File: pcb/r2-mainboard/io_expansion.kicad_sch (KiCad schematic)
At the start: 16 parts, among them J22 HC-FPC-05-09-6RLTAG, J23 HC-FPC-05-09-6RLTAG, J28 USB-C 16P, U54 TPS22914BYFPR, U55 TPS22914BYFPR, U56 TPS2553DBVR, U57 USBLC6-2SC6

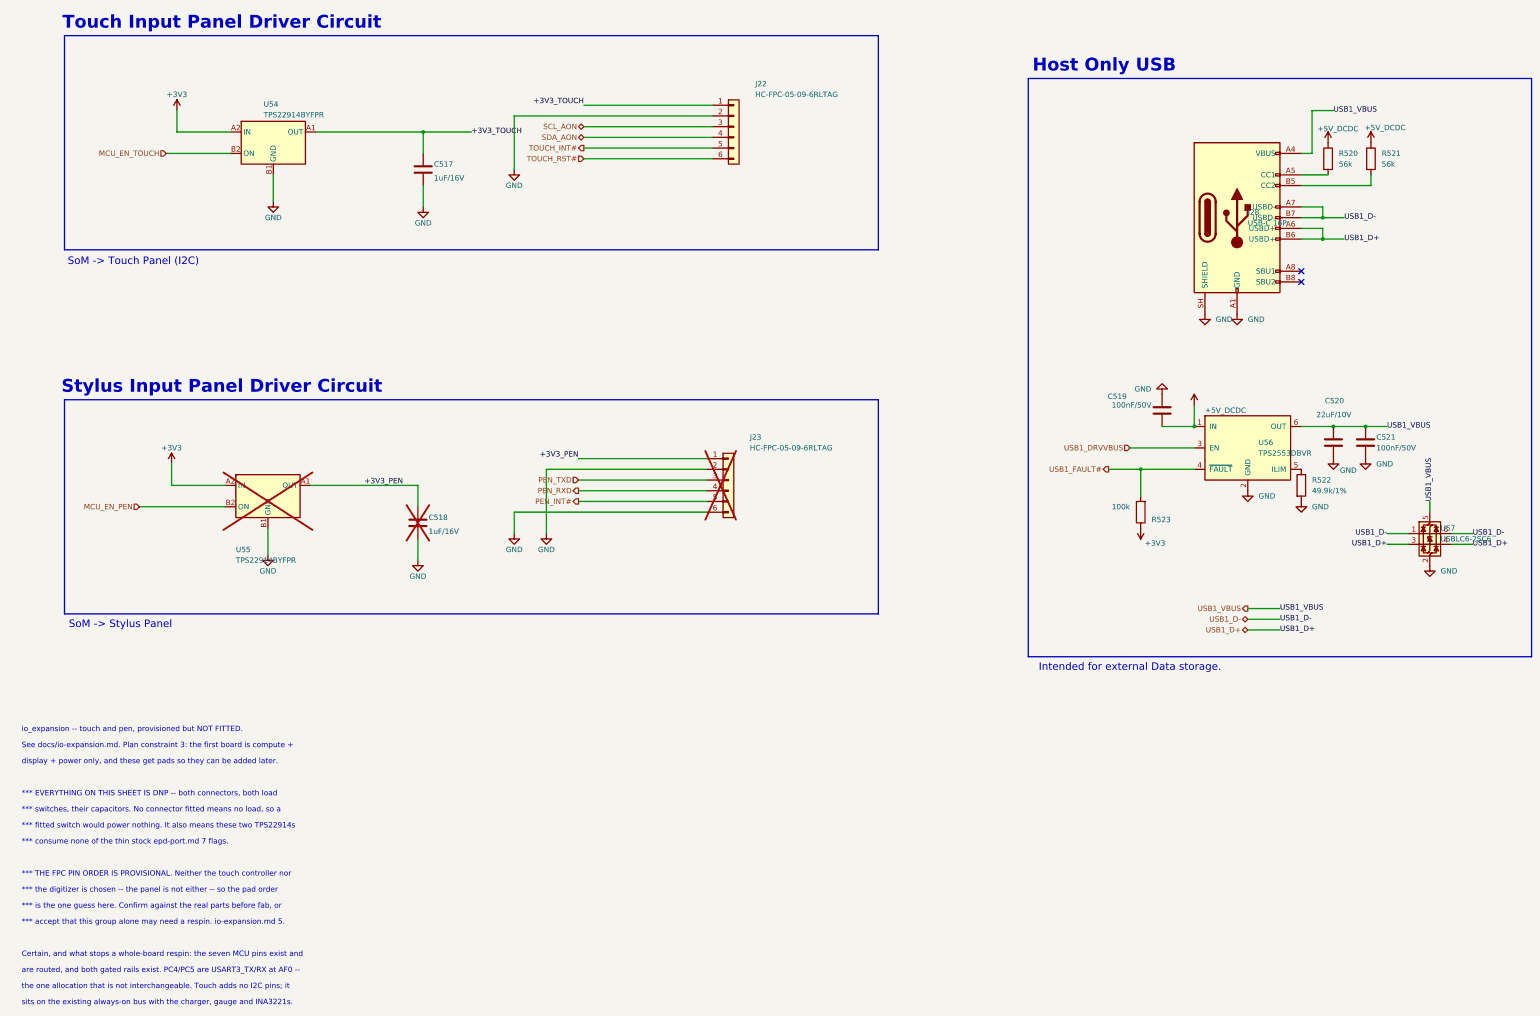
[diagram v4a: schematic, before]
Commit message: Renumber io_expansion to the page-14 scheme
The owner's designator scheme is classifier + sheet page number + a
two-digit part number, counted from 00 -- battery (page 2) is U200/J201,
power (page 3) is U300-U304, fpga_config (page 9) is U902. Pages 10-14
therefore need four digits, which the owner confirmed.

io_expansion is page 14:

  U54  -> U1400   touch load switch      J22  -> J1400   touch FPC
  U55  -> U1401   pen load switch        J23  -> J1401   pen FPC
  U56  -> U1402   TPS2553 USB switch     J28  -> J1402   USB-C host
  U57  -> U1403   USBLC6 ESD
  R520 -> R1400   CC1 pull-up            C517 -> C1400   touch rail
  R521 -> R1401   CC2 pull-up            C518 -> C1401   pen rail
  R522 -> R1402   ILIM                   C519 -> C1402   TPS2553 IN
  R523 -> R1403   FAULT pull-up          C520 -> C1403   VBUS bulk
                                         C521 -> C1404   VBUS bypass

Applied to io_expansion.kicad_sch and r2.kicad_pcb by quoted-string
match, and to the docs and tools/ by word boundary so R52 could never
eat R520. All sixteen target designators were checked free first.

Verified: 519 nets before and after, and *no* net membership changed --
the only differences are the five auto-generated names that embed a
designator (Net-(J28-CC1) -> Net-(J1402-CC1) and friends). ERC unchanged
at 14 errors / 20 warnings. Schematic and board designators agree in
both directions.

The scheme is now recorded in CLAUDE.md, including the warning that
check_pcb.py and check_ucf.py still assert on legacy names.

Co-Authored-By: Claude Opus 5 <noreply@anthropic.com>
Claude-Session: https://claude.ai/code/session_01MHTAe6ZnhogTEgtyPcLhwG
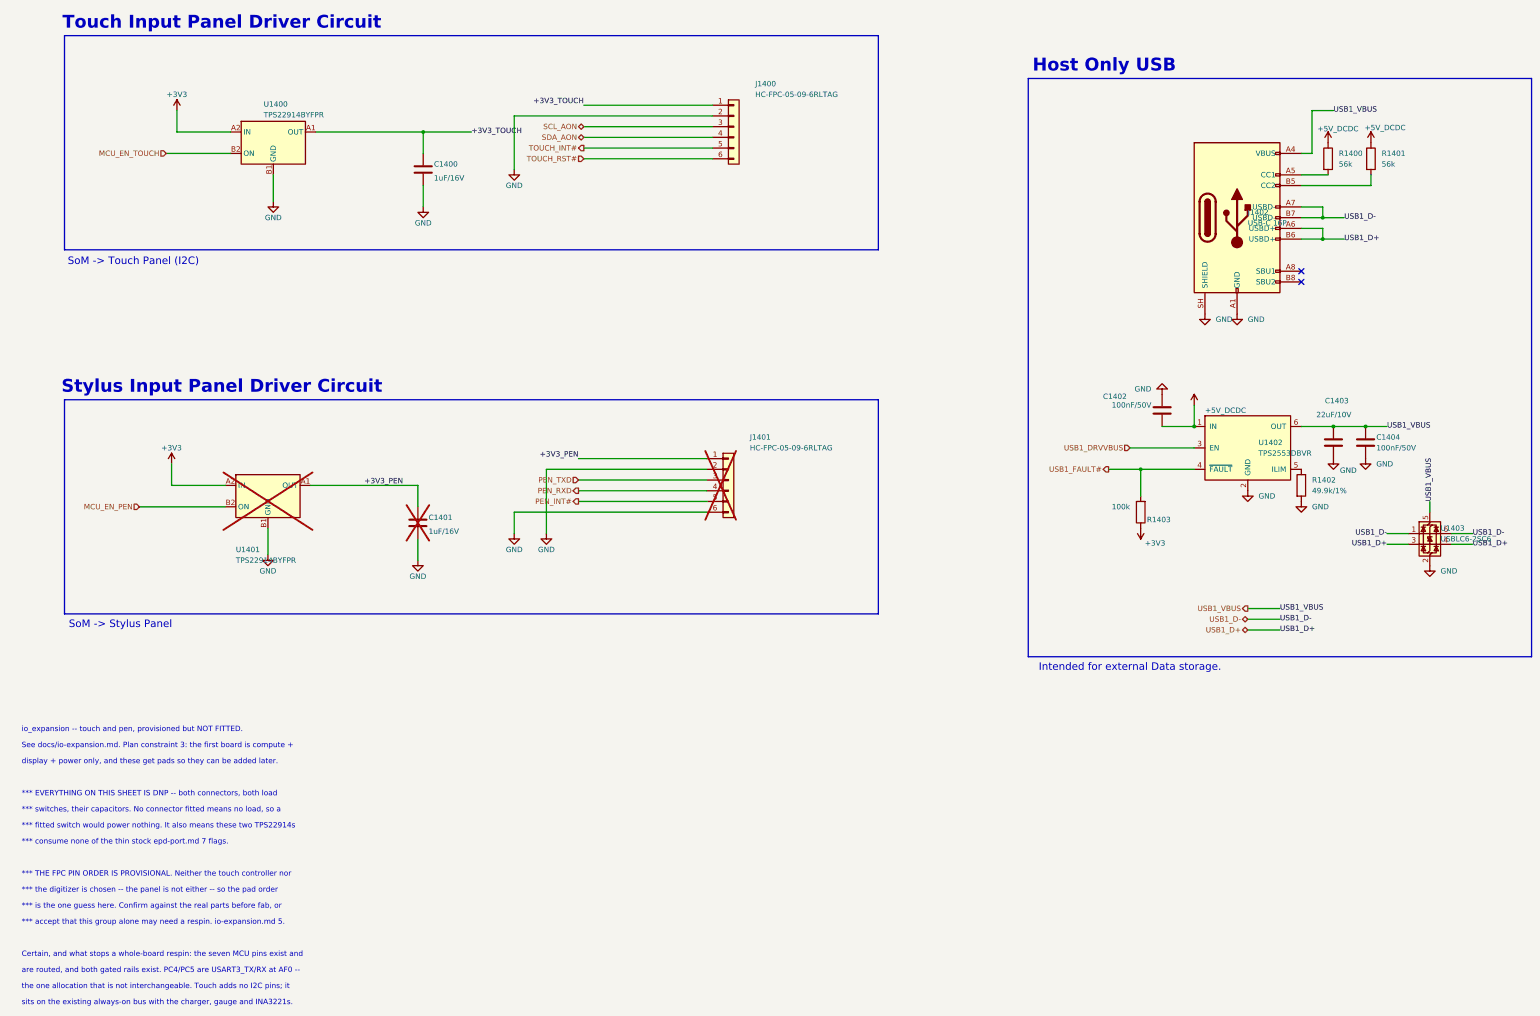
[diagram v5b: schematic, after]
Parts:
- renumbered C517 to C1400, C518 to C1401, C519 to C1402, C520 to C1403, C521 to C1404, J22 to J1400, J23 to J1401, J28 to J1402, R520 to R1400, R521 to R1401, R522 to R1402, R523 to R1403, U54 to U1400, U55 to U1401, U56 to U1402, U57 to U1403
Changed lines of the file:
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@@
 		(in_pos_files no)
 		(dnp yes)
-		(property "Reference" "U55"
+		(property "Reference" "U1401"
 			(at 71.12 167.64 0)
 			(show_name no)
@@
 			(project "r2"
 				(path "/dee825bf-c2f1-415d-afdf-cf702072a6e8/bfb4a282-c959-4a7b-92d0-a4a500453c0c"
-					(reference "U55")
+					(reference "U1401")
 					(unit 1)
 				)
@@
 		(in_pos_files yes)
 		(dnp no)
-		(property "Reference" "C517"
+		(property "Reference" "C1400"
 			(at 118.11 76.2 0)
 			(show_name no)
@@
 			(project "r2"
 				(path "/dee825bf-c2f1-415d-afdf-cf702072a6e8/bfb4a282-c959-4a7b-92d0-a4a500453c0c"
-					(reference "C517")
+					(reference "C1400")
 					(unit 1)
 				)
@@
 		(in_pos_files no)
 		(dnp yes)
-		(property "Reference" "J23"
+		(property "Reference" "J1401"
 			(at 193.04 140.97 0)
 			(show_name no)
@@
 			(project "r2"
 				(path "/dee825bf-c2f1-415d-afdf-cf702072a6e8/bfb4a282-c959-4a7b-92d0-a4a500453c0c"
-					(reference "J23")
+					(reference "J1401")
 					(unit 1)
 				)
@@
 		(in_pos_files yes)
 		(dnp no)
-		(property "Reference" "J22"
+		(property "Reference" "J1400"
 			(at 194.31 57.15 0)
 			(show_name no)
@@
 			(project "r2"
 				(path "/dee825bf-c2f1-415d-afdf-cf702072a6e8/bfb4a282-c959-4a7b-92d0-a4a500453c0c"
-					(reference "J22")
+					(reference "J1400")
 					(unit 1)
 				)
@@
 		(dnp no)
 		(fields_autoplaced yes)
-		(property "Reference" "U56"
+		(property "Reference" "U1402"
 			(at 313.69 142.24 0)
 			(show_name no)
@@
 			(project "r2"
 				(path "/dee825bf-c2f1-415d-afdf-cf702072a6e8/bfb4a282-c959-4a7b-92d0-a4a500453c0c"
-					(reference "U56")
+					(reference "U1402")
 					(unit 1)
 				)
@@
 		(in_pos_files no)
 		(dnp yes)
-		(property "Reference" "C518"
+		(property "Reference" "C1401"
 			(at 116.84 160.02 0)
 			(show_name no)
@@
 			(project "r2"
 				(path "/dee825bf-c2f1-415d-afdf-cf702072a6e8/bfb4a282-c959-4a7b-92d0-a4a500453c0c"
-					(reference "C518")
+					(reference "C1401")
 					(unit 1)
 				)
@@
 		(dnp no)
 		(fields_autoplaced yes)
-		(property "Reference" "R522"
+		(property "Reference" "R1402"
 			(at 326.39 151.13 0)
 			(show_name no)
@@
 			(project "r2"
 				(path "/dee825bf-c2f1-415d-afdf-cf702072a6e8/bfb4a282-c959-4a7b-92d0-a4a500453c0c"
-					(reference "R522")
+					(reference "R1402")
 					(unit 1)
 				)
@@
 		(dnp no)
 		(fields_autoplaced yes)
-		(property "Reference" "R520"
+		(property "Reference" "R1400"
 			(at 332.74 73.66 0)
 			(show_name no)
@@
 			(project "r2"
 				(path "/dee825bf-c2f1-415d-afdf-cf702072a6e8/bfb4a282-c959-4a7b-92d0-a4a500453c0c"
-					(reference "R520")
+					(reference "R1400")
 					(unit 1)
 				)
@@
 		(in_pos_files yes)
 		(dnp no)
-		(property "Reference" "R523"
+		(property "Reference" "R1403"
 			(at 292.862 160.528 0)
 			(show_name no)
@@
 			(project "r2"
 				(path "/dee825bf-c2f1-415d-afdf-cf702072a6e8/bfb4a282-c959-4a7b-92d0-a4a500453c0c"
-					(reference "R523")
+					(reference "R1403")
 					(unit 1)
 				)
@@
 		(in_pos_files yes)
 		(dnp no)
-		(property "Reference" "C519"
+		(property "Reference" "C1402"
 			(at 282.448 131.318 0)
 			(show_name no)
@@
 			(project "r2"
 				(path "/dee825bf-c2f1-415d-afdf-cf702072a6e8/bfb4a282-c959-4a7b-92d0-a4a500453c0c"
-					(reference "C519")
+					(reference "C1402")
 					(unit 1)
 				)
@@
 		(in_pos_files yes)
 		(dnp no)
-		(property "Reference" "U54"
+		(property "Reference" "U1400"
 			(at 77.724 61.976 0)
 			(show_name no)
@@
 			(project "r2"
 				(path "/dee825bf-c2f1-415d-afdf-cf702072a6e8/bfb4a282-c959-4a7b-92d0-a4a500453c0c"
-					(reference "U54")
+					(reference "U1400")
 					(unit 1)
 				)
@@
 		(in_pos_files yes)
 		(dnp no)
-		(property "Reference" "C520"
+		(property "Reference" "C1403"
 			(at 329.438 132.334 0)
 			(show_name no)
@@
 			(project "r2"
 				(path "/dee825bf-c2f1-415d-afdf-cf702072a6e8/bfb4a282-c959-4a7b-92d0-a4a500453c0c"
-					(reference "C520")
+					(reference "C1403")
 					(unit 1)
 				)
@@
 		(dnp no)
 		(fields_autoplaced yes)
-		(property "Reference" "J28"
+		(property "Reference" "J1402"
 			(at 311.15 87.63 0)
 			(show_name no)
@@
 			(project "r2"
 				(path "/dee825bf-c2f1-415d-afdf-cf702072a6e8/bfb4a282-c959-4a7b-92d0-a4a500453c0c"
-					(reference "J28")
+					(reference "J1402")
 					(unit 1)
 				)
@@
 		(dnp no)
 		(fields_autoplaced yes)
-		(property "Reference" "U57"
+		(property "Reference" "U1403"
 			(at 356.87 162.56 0)
 			(show_name no)
@@
 			(project "r2"
 				(path "/dee825bf-c2f1-415d-afdf-cf702072a6e8/bfb4a282-c959-4a7b-92d0-a4a500453c0c"
-					(reference "U57")
+					(reference "U1403")
 					(unit 1)
 				)
@@
 		(dnp no)
 		(fields_autoplaced yes)
-		(property "Reference" "C521"
+		(property "Reference" "C1404"
 			(at 341.63 140.97 0)
 			(show_name no)
@@
 			(project "r2"
 				(path "/dee825bf-c2f1-415d-afdf-cf702072a6e8/bfb4a282-c959-4a7b-92d0-a4a500453c0c"
-					(reference "C521")
+					(reference "C1404")
 					(unit 1)
 				)
@@
 		(dnp no)
 		(fields_autoplaced yes)
-		(property "Reference" "R521"
+		(property "Reference" "R1401"
 			(at 342.9 73.66 0)
 			(show_name no)
@@
 			(project "r2"
 				(path "/dee825bf-c2f1-415d-afdf-cf702072a6e8/bfb4a282-c959-4a7b-92d0-a4a500453c0c"
-					(reference "R521")
-					(unit 1)
-				)
+					(reference "R1401")
+					(unit 1)
+				)
